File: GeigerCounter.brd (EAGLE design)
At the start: 69.9 x 54.6 mm, 40 parts, among them IC1 TLC555CP, IC2 ATtiny2313A-SU, J1 LND 712, J2 I2C, J3 ICSP, J4 I/O, Q1 STN83003, Q2 MMBT2222ALT3G, Q3 MMBT2222ALT3G, Q4 8 MHz, Q5 SMD Buzzer

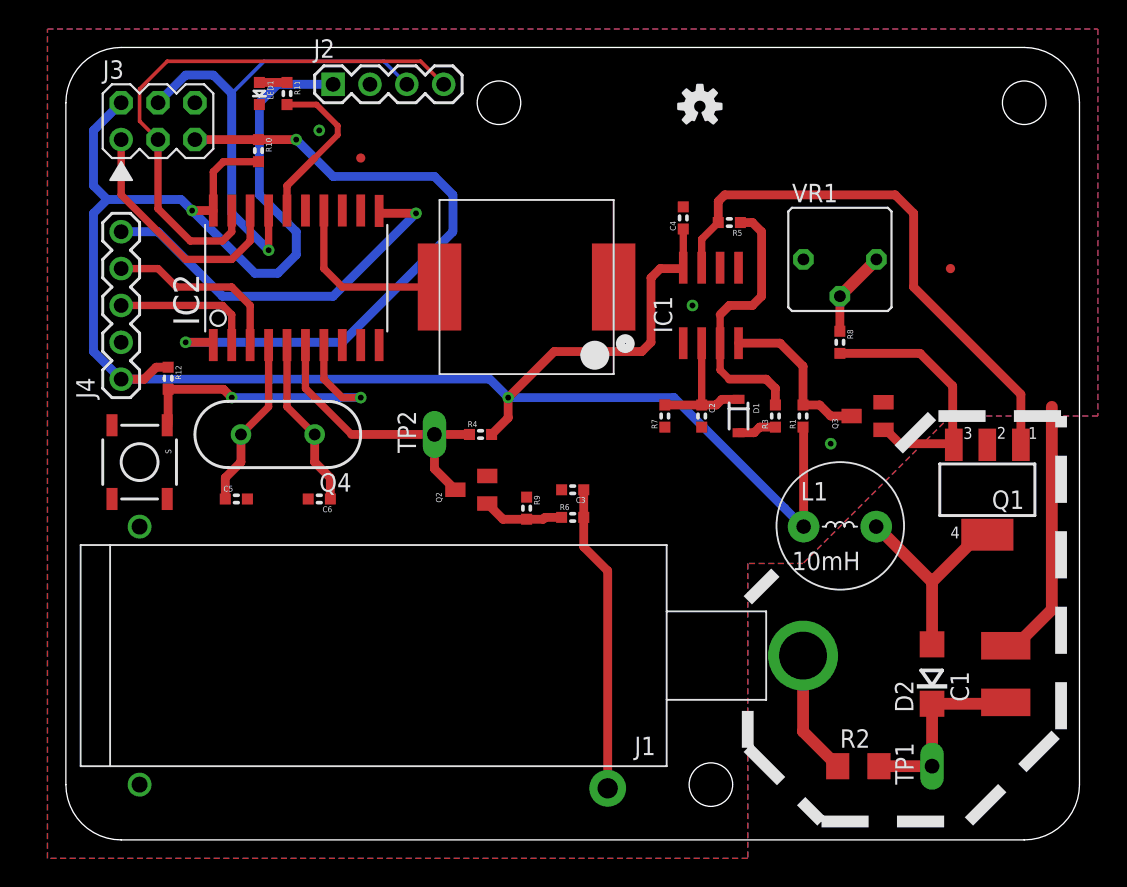
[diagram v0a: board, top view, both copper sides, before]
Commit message: silkscreen tweaks
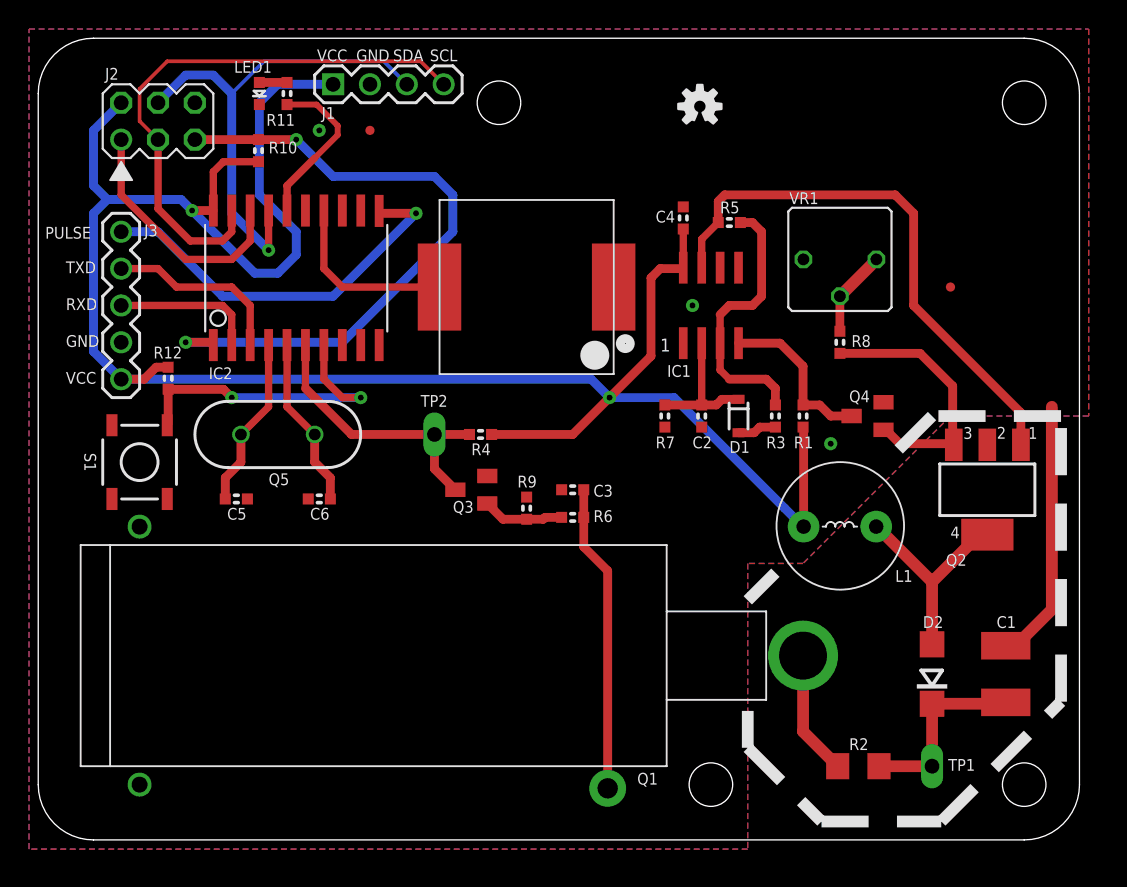
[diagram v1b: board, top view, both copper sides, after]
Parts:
- removed J4: I/O, freetronics-master-v1:1X05
- added Q6: SMD Buzzer, freetronics-master-v1:BUZZER-12X12-SMT
- J1: value LND 712 -> I2C; device SparkFun:GEIGER_TUBE -> freetronics-master-v1:1X04
- J2: value I2C -> ICSP; device freetronics-master-v1:1X04 -> connectors:ICSP-6
- J3: value ICSP -> I/O; device connectors:ICSP-6 -> freetronics-master-v1:1X05
- Q1: value STN83003 -> LND 712; device transistor-neu-to92:SOT223 -> SparkFun:GEIGER_TUBE
- Q2: value MMBT2222ALT3G -> STN83003; device SparkFun:SOT23 -> transistor-neu-to92:SOT223
- Q4: value 8 MHz -> MMBT2222ALT3G; device freetronics-master-v1:HC49US -> SparkFun:SOT23
- Q5: value SMD Buzzer -> 8 MHz; device freetronics-master-v1:BUZZER-12X12-SMT -> freetronics-master-v1:HC49US
- R9: value 100kΩ -> 100k
- moved J1 51.0 mm to (19.7, 53.3), turned to 0 degrees
- moved Q4 40.7 mm to (56.5, 30.5), turned to 90 degrees
- moved Q2 35.6 mm to (64.8, 25.4), turned to 180 degrees
- moved Q3 27.8 mm to (29.2, 25.4)
- moved Q5 19.9 mm to (15.9, 29.2)
- moved J3 18.0 mm to (5.08, 33.0), turned to 90 degrees
- moved Q1 17.1 mm to (52.1, 14.0)
- moved J2 12.3 mm to (7.62, 50.8)
- moved JP2 2.01 mm to (22.2, 50.2)
- moved JP1 1.27 mm to (62.2, 39.4)
- renumbered S to S1
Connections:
- net !RESET: now also J2.5; no longer J3.5
- net +3V3: now also J1.1, J2.2, J3.1; no longer J2.1, J3.2, J4.1
- net GM_PULSE: now also Q3.3; no longer Q2.3
- net GND: now also J1.2, J2.6, J3.2, Q4.2, Q6.1; no longer J2.2, J3.6, J4.2, Q2.2, Q5.1
- net N$1: now also Q1.VCC; no longer J1.VCC
- net N$14: now also Q2.1; no longer Q1.1
- net N$15: now also Q4.3; no longer Q3.3
- net N$26: now also J3.3; no longer J4.3
- net N$27: now also J3.4; no longer J4.4
- net N$28: now also Q5.1; no longer Q4.1
- net N$29: now also Q5.2; no longer Q4.2
- net N$31: now also J2.1; no longer J3.1
- net N$35: now also Q6.2; no longer Q5.2
- net N$48: now also Q1.GND; no longer J1.GND
- net N$49: now also Q3.1; no longer Q2.1
- net N$55: now also Q2.3, Q4.1; no longer Q1.3, Q3.1
- net N$57: now also Q2.4; no longer Q1.4
- net PULSE: now also J3.5; no longer J4.5
- net SCL: now also J1.4, J2.3; no longer J2.4, J3.3
- net SDA: now also J1.3, J2.4; no longer J2.3, J3.4
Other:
- board size 69.9 x 54.6 mm -> 71.8 x 55.2 mm
- board text added: "1"
- board text added: "GND"
- board text added: "PULSE"
- board text added: "RXD"
- board text added: "SCL"
- board text added: "SDA"
- board text added: "TXD"
- board text added: "VCC"
